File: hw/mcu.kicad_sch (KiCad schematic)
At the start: 16 parts, among them U2 STM32G473RCTx

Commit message: add inverter-stage
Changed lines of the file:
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@@
 (kicad_sch
-	(version 20260306)
+	(version 20260826)
 	(generator "eeschema")
-	(generator_version "10.0")
+	(generator_version "10.99")
 	(paper "A4")
 	(rectangle
@@
 			(font
 				(size 1.27 1.27)
-				(thickness 0.254)
+				(thickness 0.1588)
 				(bold yes)
 				(color 0 0 132 1)
@@
 			(font
 				(size 1.27 1.27)
-				(thickness 0.254)
+				(thickness 0.1588)
 				(bold yes)
 				(color 0 0 132 1)
@@
 			(font
 				(size 1.27 1.27)
-				(thickness 0.254)
+				(thickness 0.1588)
 				(bold yes)
 				(color 0 0 132 1)

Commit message: basic *.kicad_sch done
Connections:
- net DRV_EN: now also U2.33 (PB11); no longer U2.38 (PC6)
- net BUTTON_A renamed I2C1_PULLUP
- net BUTTON_B renamed I2C4_PULLUP
- net LED_STATUS renamed STATUS_LED
- net PA2 renamed AUX1
- net PA3 renamed AUX2
- net PA6 renamed AUX3
- net PB7 renamed AUX6
- net PB8 renamed AUX7
- net PB9 renamed AUX8
- net PC4 renamed AUX4
- net PC5 renamed AUX5
- net SENSE_VBUS renamed SENSE_VBAT
- new net AUX9: U2.38 (PC6)
- no-connect marks 6 -> 5
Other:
- note removed: "Button"
- moved on the sheet: TP10, TP11, TP12, TP13, TP14, TP15, TP5, TP6, TP7, TP8, TP9

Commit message: began with lcsc and footprints
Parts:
- renumbered U2 to U1
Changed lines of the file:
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@@
 		(in_pos_files yes)
 		(dnp no)
-		(property "Reference" "U2"
+		(property "Reference" "U1"
 			(at 47.244 28.194 0)
 			(show_name no)
@@
 			(project "atlas-electronics"
 				(path "/915bc1ff-7be5-4368-a2db-c4889af73afd/f55389d3-e940-4fdc-b600-a2530eb9690b"
-					(reference "U2")
+					(reference "U1")
 					(unit 2)
 				)

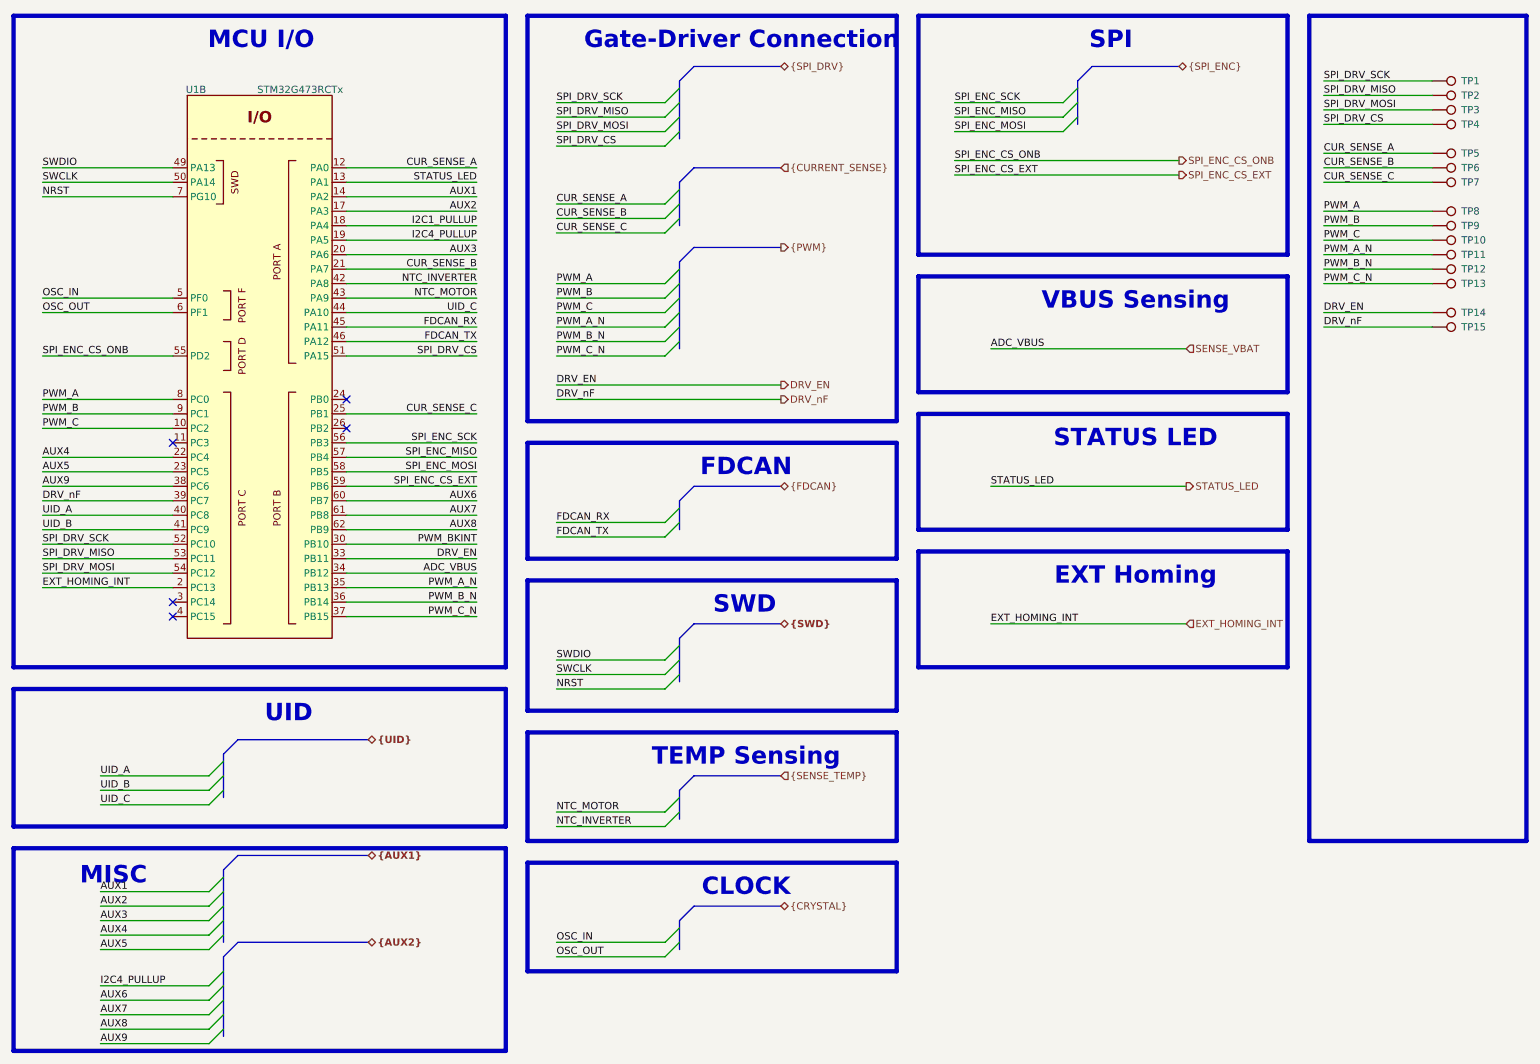
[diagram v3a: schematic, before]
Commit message: cleaned up *.kicad_sch
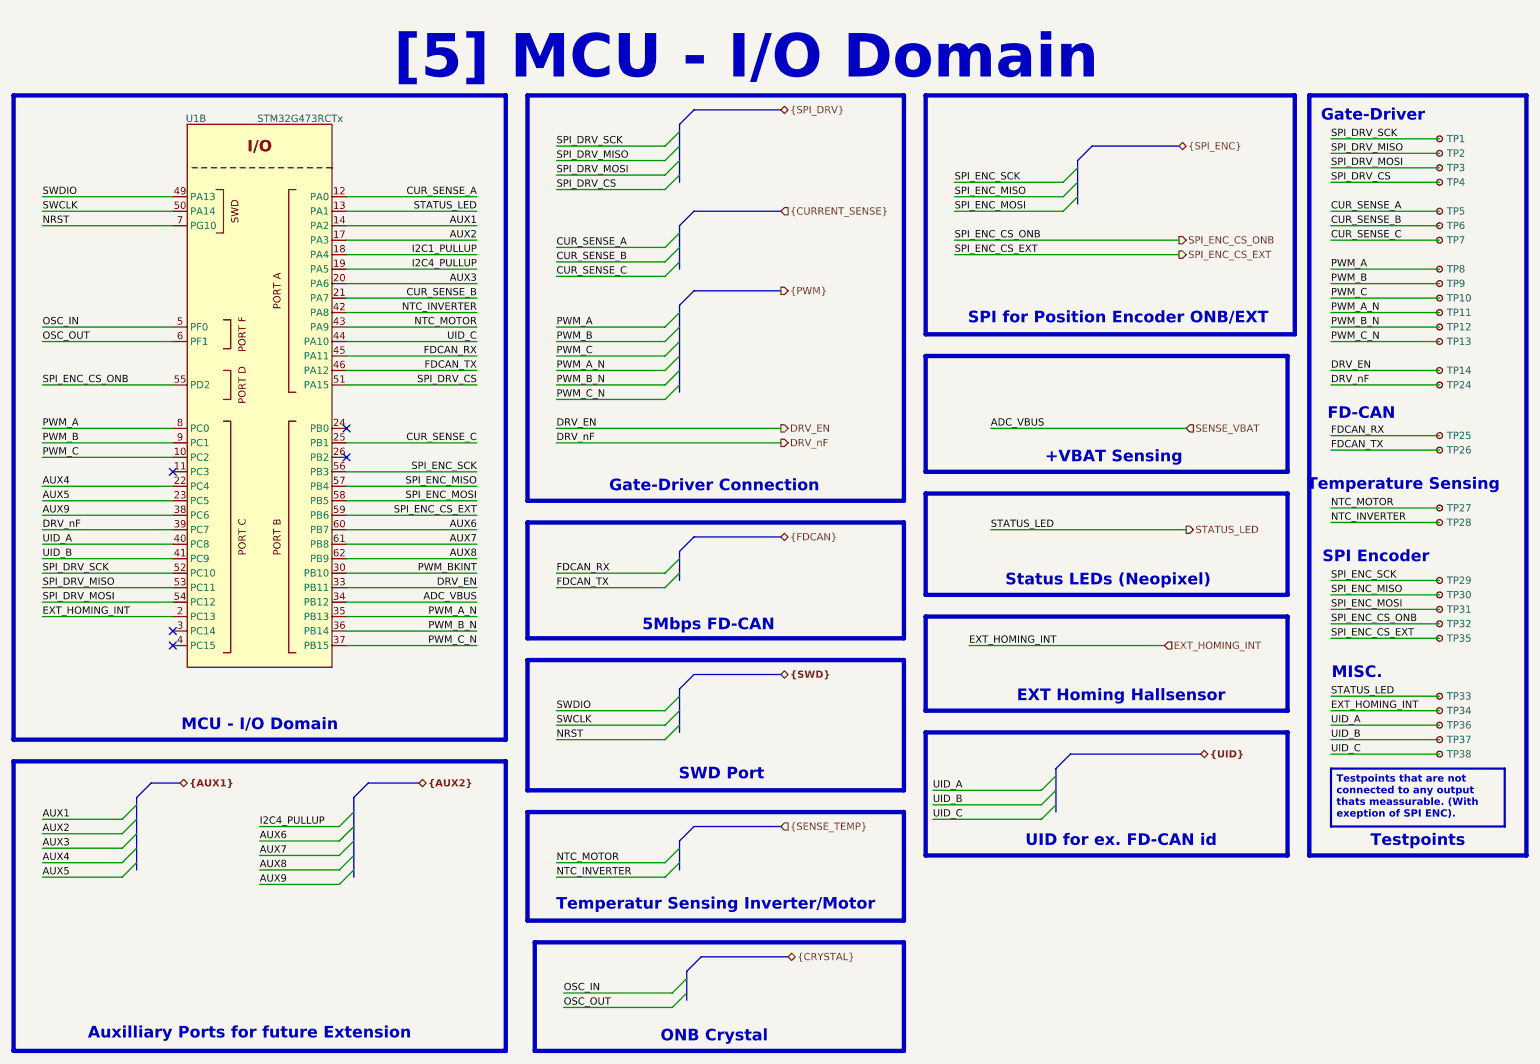
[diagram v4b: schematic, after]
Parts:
- removed TP1, TP10, TP11, TP12, TP13, TP14, TP15, TP2, TP3, TP4, TP5, TP6, TP7, TP8, TP9: TestPoint, symbol Connector:TestPoint
- added TP1, TP10, TP11, TP12, TP13, TP14, TP2, TP24, TP25, TP26, TP27, TP28, TP29, TP3, TP30, TP31, TP32, TP33, TP34, TP35, TP36, TP37, TP38, TP4, TP5, TP6, TP7, TP8, TP9: TestPoint_Small, TestPoint:TestPoint_Pad_D1.0mm, symbol Connector:TestPoint_Small
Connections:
- net CUR_SENSE_A: now also TP5.1
- net CUR_SENSE_B: now also TP6.1
- net CUR_SENSE_C: now also TP7.1
- net DRV_EN: now also TP14.1
- net DRV_nF: now also TP24.1
- net EXT_HOMING_INT: now also TP34.1
- net FDCAN_RX: now also TP25.1
- net FDCAN_TX: now also TP26.1
- net NTC_INVERTER: now also TP28.1
- net NTC_MOTOR: now also TP27.1
- net PWM_A: now also TP8.1
- net PWM_A_N: now also TP11.1
- net PWM_B: now also TP9.1
- net PWM_B_N: now also TP12.1
- net PWM_C: now also TP10.1
- net PWM_C_N: now also TP13.1
- net SPI_DRV_CS: now also TP4.1
- net SPI_DRV_MISO: now also TP2.1
- net SPI_DRV_MOSI: now also TP3.1
- net SPI_DRV_SCK: now also TP1.1
- net SPI_ENC_CS_EXT: now also TP35.1
- net SPI_ENC_CS_ONB: now also TP32.1
- net SPI_ENC_MISO: now also TP30.1
- net SPI_ENC_MOSI: now also TP31.1
- net SPI_ENC_SCK: now also TP29.1
- net STATUS_LED: now also TP33.1
- net UID_A: now also TP36.1
- net UID_B: now also TP37.1
- net UID_C: now also TP38.1
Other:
- note added: "+VBAT Sensing"
- note added: "5Mbps FD-CAN"
- note added: "Auxilliary Ports for future Extension"
- note added: "EXT Homing Hallsensor"
- note added: "FD-CAN"
- note added: "Gate-Driver"
- note added: "MCU - I/O Domain"
- note added: "MISC."
- note added: "ONB Crystal"
- note added: "SPI Encoder"
- note added: "SPI for Position Encoder ONB/EXT"
- note added: "SWD Port"
- note added: "Status LEDs (Neopixel)"
- note added: "Temperatur Sensing Inverter/Motor"
- note added: "Temperature Sensing"
- note added: "Testpoints"
- note added: "UID for ex. FD-CAN id"
- note added: "[5] MCU - I/O Domain"
- note removed: "CLOCK"
- note removed: "EXT Homing"
- note removed: "FDCAN"
- note removed: "MCU I/O"
- note removed: "MISC"
- note removed: "SPI"
- note removed: "STATUS LED"
- note removed: "SWD"
- note removed: "TEMP Sensing"
- note removed: "UID"
- note removed: "VBUS Sensing"
- title: (none) -> MCU - IO Domain
- moved on the sheet: U1B
